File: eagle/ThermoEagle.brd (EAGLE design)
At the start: 100 x 80 mm, 35 parts, among them IC1 MAX232, IC2 4511N, Q1 20MHz, T1 2N2219, T2 2N2219, U1 LM324

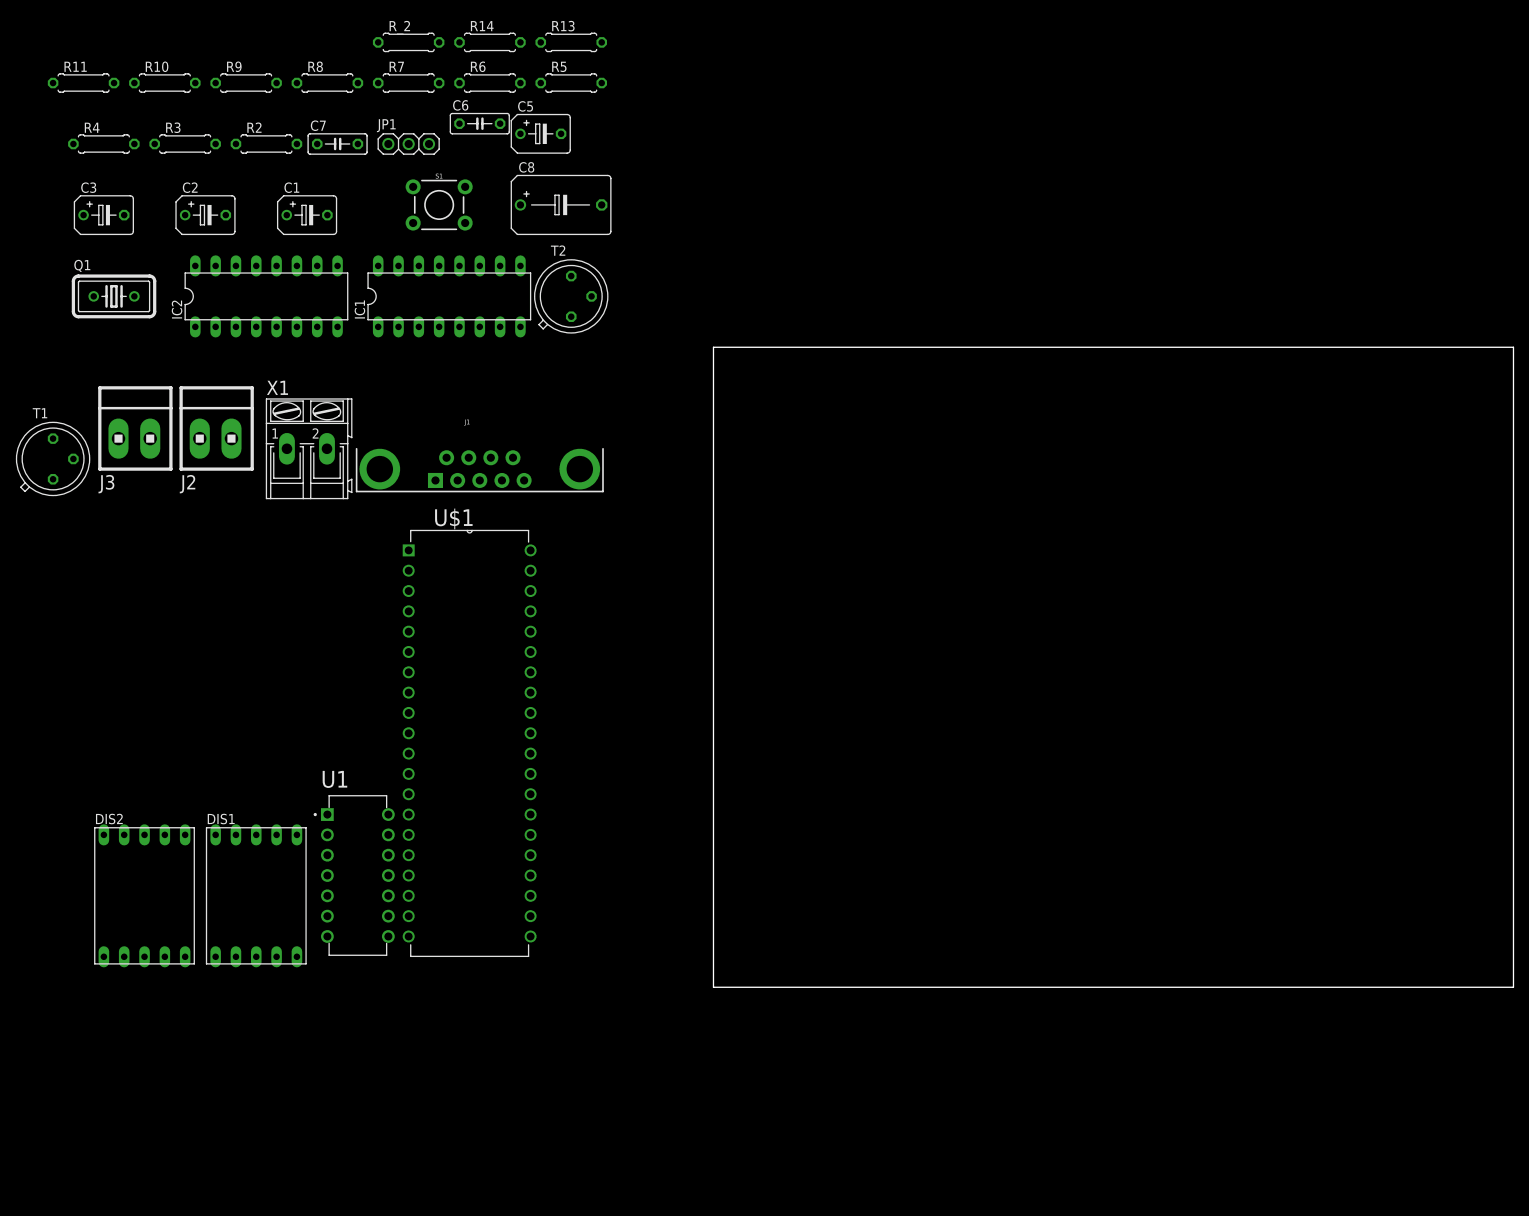
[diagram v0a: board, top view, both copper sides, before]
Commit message: Update ThermoEagle board
Updated the board to match the new Schematic file from Eagle.
Made the blue circuit but still need to perform the mass.
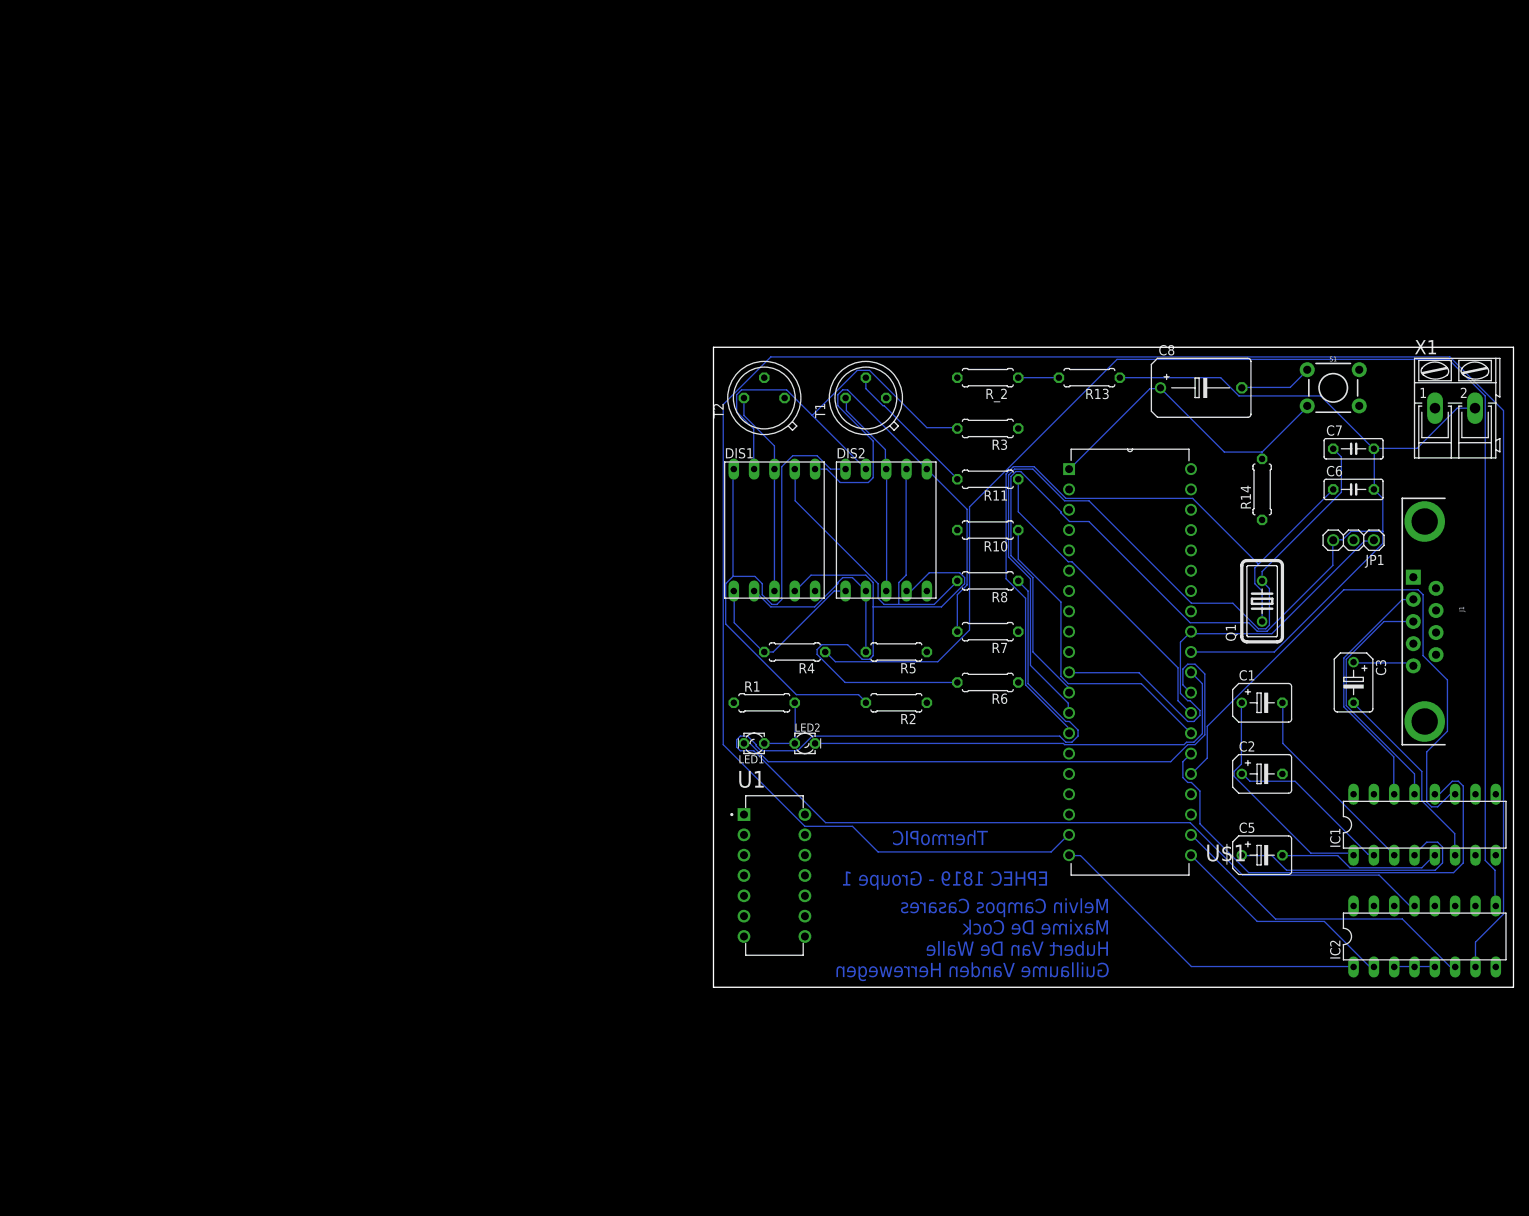
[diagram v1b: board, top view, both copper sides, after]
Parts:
- removed J2, J3: (no value), con-amp:1X2MTA
- removed R9: 470K, resistor:0207/7
- added LED1, LED2: (no value), eagle-ltspice:LED_LD260
- added R1: 470K, resistor:0207/7
- moved C3 166.8 mm to (80.0, 38.1), turned to 270 degrees
- moved IC2 165.4 mm to (88.9, 6.35)
- moved C2 149.4 mm to (68.6, 26.7)
- moved Q1 148.5 mm to (68.6, 48.3), turned to 90 degrees
- moved X1 143.6 mm to (92.7, 72.4)
- moved IC1 138.7 mm to (88.9, 20.3)
- moved C1 134.0 mm to (68.6, 35.6)
- moved C7 132.6 mm to (80.0, 67.3)
- moved JP1 128.1 mm to (80.0, 55.9), turned to 180 degrees
- moved C5 127.5 mm to (68.6, 16.5)
- moved R11 123.4 mm to (34.3, 63.5), turned to 180 degrees
- moved J1 119.6 mm to (88.9, 45.7), turned to 270 degrees
- moved C6 118.4 mm to (80.0, 62.2)
- moved R10 117.1 mm to (34.3, 57.1), turned to 180 degrees
- moved S1 114.1 mm to (77.5, 74.9)
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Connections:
- removed net A: U$1.33
- removed net B: U$1.34
- removed net C: U$1.35
- removed net D: U$1.36
- removed net N$2 (its old number): J2.2, U$1.21
- removed net N$47: U$1.31
- removed net N$51: R13.1
- removed net N$54: C6.2, C7.2
- removed net N$58: IC2.1
- removed net N$59: IC2.2
- removed net N$60: IC2.6
- new net N$23: LED1.A, LED2.A, R1.2
- net GND: now also C6.2, C7.2, R13.1, U$1.12, U$1.31
- net N$1: now also IC2.7, U$1.19; no longer DIS2.5, R9.2
- net N$11: now also IC2.2, U$1.21; no longer IC2.3, IC2.4, R9.1, U$1.19
- net N$22: now also IC2.6, U$1.22; no longer IC2.7
- net N$37: now also LED2.K, U$1.30; no longer J3.2, R10.1
- net N$38: now also R10.1, U$1.27; no longer J2.1, R11.1
- net N$44: now also R11.1, U$1.28; no longer U$1.11
- net N$45: now also LED1.K, U$1.29; no longer U$1.32
- net N$46: now also R1.1; no longer U$1.12
- net N$5: now also IC2.3, IC2.4, IC2.5; no longer J3.1, U$1.20
- net N$6: now also IC2.1, U$1.20; no longer IC2.5
- net VCC: now also U$1.11, U$1.32
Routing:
- net N$1: track 0.00 -> 266.0 mm
- net GND: track 0.00 -> 184.2 mm
- net N$29: track 0.00 -> 173.9 mm
- net N$31: track 0.00 -> 161.8 mm
- net N$53: track 0.00 -> 101.3 mm
- net N$52: track 0.00 -> 93.6 mm
- net N$36: track 0.00 -> 76.0 mm
- net N$45: track 0.00 -> 74.5 mm
- net N$41: track 0.00 -> 73.8 mm
- net N$26: track 0.00 -> 69.8 mm
- net RX: track 0.00 -> 60.4 mm
- net VCC: track 0.00 -> 59.2 mm
- net N$27: track 0.00 -> 58.8 mm
- net N$37: track 0.00 -> 57.3 mm
- net N$10: track 0.00 -> 54.3 mm
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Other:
- board text added: "EPHEC 1819 - Groupe 1"
- board text added: "Melvin Campos Casares Maxime De Cock Hubert Van De Walle Guillaume Vanden Herrewegen"
- board text added: "ThermoPIC"

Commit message: Eagle to fix by Maxime
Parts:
- removed J1: (no value), SparkFun-Connectors:DB9
- removed R_2: (no value), resistor:0207/7
- added J2: (no value), con-amp:10X03MTA
- added X2: (no value), con-subd:F09VB
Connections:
- net N$2: no longer J1.2
- net N$20: no longer J1.5
- net N$21: no longer J1.3
- net N$49: no longer R_2.2
- net N$50: no longer R_2.1
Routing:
- net N$50: track 5.08 -> 0.00 mm
- net N$21: track 30.7 -> 27.1 mm
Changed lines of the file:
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@@
 <attribute name="VALUE" x="81.407" y="5.715" size="1.27" layer="27" ratio="10"/>
-</element>
-<element name="J1" library="SparkFun-Connectors" library_urn="urn:adsk.eagle:library:513" package="DB9" package3d_urn="urn:adsk.eagle:package:38025/1" value="" x="88.9" y="45.72" smashed="yes" rot="R270">
-<attribute name="NAME" x="93.218" y="47.625" size="0.6096" layer="25" font="vector" ratio="20" rot="R270"/>
-<attribute name="PROD_ID" value="CONN-08194" x="24.13" y="16.51" size="1.778" layer="27" rot="R270" display="off"/>
-<attribute name="VALUE" x="93.472" y="47.625" size="0.6096" layer="27" font="vector" ratio="20" rot="R270"/>
 </element>
 <element name="JP1" library="adafruit" library_urn="urn:adsk.eagle:library:420" package="1X03" package3d_urn="urn:adsk.eagle:package:6240710/1" value="" x="80.01" y="55.88" smashed="yes" rot="R180">
@@
 <attribute name="NAME" x="36.83" y="49.403" size="1.27" layer="25" ratio="10" rot="R180"/>
 <attribute name="VALUE" x="36.576" y="51.3588" size="1.27" layer="27" ratio="10" rot="R180"/>
-</element>
-<element name="R_2" library="resistor" library_urn="urn:adsk.eagle:library:348" package="0207/7" package3d_urn="urn:adsk.eagle:package:23493/2" value="" x="34.29" y="76.2" smashed="yes" rot="R180">
-<attribute name="NAME" x="36.83" y="74.803" size="1.27" layer="25" ratio="10" rot="R180"/>
-<attribute name="VALUE" x="36.576" y="76.7588" size="1.27" layer="27" ratio="10" rot="R180"/>
 </element>
 <element name="S1" library="SparkFun-Switches" library_urn="urn:adsk.eagle:library:535" package="TACTILE_SWITCH_PTH_6.0MM" package3d_urn="urn:adsk.eagle:package:40163/1" value="MOMENTARY-SWITCH-SPST-PTH-6.0MM" x="77.47" y="74.93" smashed="yes">
@@
 <attribute name="OC_NEWARK" value="unknown" x="143.51" y="5.08" size="1.778" layer="27" display="off"/>
 <attribute name="VALUE" x="87.63" y="63.754" size="1.778" layer="27" ratio="10"/>
+</element>
+<element name="J2" library="con-amp" library_urn="urn:adsk.eagle:library:127" package="10X03MTA" package3d_urn="urn:adsk.eagle:package:8081621/1" value="" x="3.81" y="-5.08" smashed="yes">
+<attribute name="NAME" x="1.1938" y="-8.3312" size="1.27" layer="25"/>
+<attribute name="VALUE" x="0.0338" y="-2.9291" size="1.27" layer="27"/>
+</element>
+<element name="X2" library="con-subd" library_urn="urn:adsk.eagle:library:189" package="F09VB" package3d_urn="urn:adsk.eagle:package:10282/1" value="" x="16.51" y="-20.32" smashed="yes">
+<attribute name="MF" value="" x="16.51" y="-20.32" size="1.778" layer="27" display="off"/>
+<attribute name="MPN" value="" x="16.51" y="-20.32" size="1.778" layer="27" display="off"/>
+<attribute name="NAME" x="1.143" y="-12.065" size="1.778" layer="25" ratio="10"/>
+<attribute name="OC_FARNELL" value="unknown" x="16.51" y="-20.32" size="1.778" layer="27" display="off"/>
+<attribute name="OC_NEWARK" value="unknown" x="16.51" y="-20.32" size="1.778" layer="27" display="off"/>
+<attribute name="VALUE" x="16.51" y="-12.065" size="1.778" layer="27" ratio="10"/>
 </element>
 </elements>
@@
 </signal>
 <signal name="N$21">
-<contactref element="J1" pad="3"/>
 <contactref element="IC1" pad="13"/>
 <wire x1="87.63" y1="26.67" x2="87.63" y2="24.13" width="0.1524" layer="16"/>
@@
 <wire x1="79.0956" y1="40.9956" x2="79.0956" y2="35.2044" width="0.1524" layer="16"/>
 <wire x1="83.82" y1="45.72" x2="79.0956" y2="40.9956" width="0.1524" layer="16"/>
-<wire x1="87.48" y1="45.72" x2="83.82" y2="45.72" width="0.1524" layer="16"/>
 </signal>
 <signal name="N$20">
-<contactref element="J1" pad="5"/>
 <contactref element="C3" pad="+"/>
 <wire x1="87.1728" y1="40.5384" x2="80.01" y2="40.5384" width="0.1524" layer="16"/>
 <wire x1="87.4776" y1="40.2336" x2="87.1728" y2="40.5384" width="0.1524" layer="16"/>
 <wire x1="80.01" y1="40.5384" x2="80.01" y2="40.64" width="0.1524" layer="16"/>
-<wire x1="87.4776" y1="40.2336" x2="87.48" y2="40.18" width="0.1524" layer="16"/>
 </signal>
 <signal name="N$4">
@@
 <signal name="N$49">
 <contactref element="U1" pad="1"/>
-<contactref element="R_2" pad="2"/>
 <contactref element="U$1" pad="2"/>
-<wire x1="44.45" y1="62.23" x2="30.48" y2="76.2" width="0" layer="19" extent="1-1"/>
 <wire x1="3.81" y1="21.59" x2="44.45" y2="62.23" width="0" layer="19" extent="1-1"/>
 </signal>
 <signal name="N$50">
-<contactref element="R_2" pad="1"/>
 <contactref element="R13" pad="2"/>
 <contactref element="U1" pad="2"/>
-<wire x1="43.18" y1="76.2" x2="38.1" y2="76.2" width="0.1524" layer="16"/>
-<wire x1="3.81" y1="19.05" x2="38.1" y2="76.2" width="0" layer="19" extent="1-1"/>
+<wire x1="3.81" y1="19.05" x2="43.18" y2="76.2" width="0" layer="19" extent="1-1"/>
 </signal>
 <signal name="N$52">
@@
 </signal>
 <signal name="N$2">
-<contactref element="J1" pad="2"/>
 <contactref element="IC1" pad="14"/>
 <wire x1="85.0392" y1="28.8036" x2="85.0392" y2="24.2316" width="0.1524" layer="16"/>
@@
 <wire x1="87.4776" y1="48.4632" x2="86.106" y2="48.4632" width="0.1524" layer="16"/>
 <wire x1="85.0392" y1="24.2316" x2="85.09" y2="24.13" width="0.1524" layer="16"/>
-<wire x1="87.4776" y1="48.4632" x2="87.48" y2="48.49" width="0.1524" layer="16"/>
 </signal>
 <signal name="N$1">
